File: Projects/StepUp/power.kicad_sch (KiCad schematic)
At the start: 56 parts, among them J10 Conn_02x03_Odd_Even, J11 Conn_01x02, J6 Conn_01x02, J7 Conn_01x02, J8 Conn_01x02, J9 Conn_01x02, Q3 PMF170XP,115, Q4 BSS83P, U6 LDL1117S33R, U7 MCP73832T-2ACI_OT, U8 MIC2253

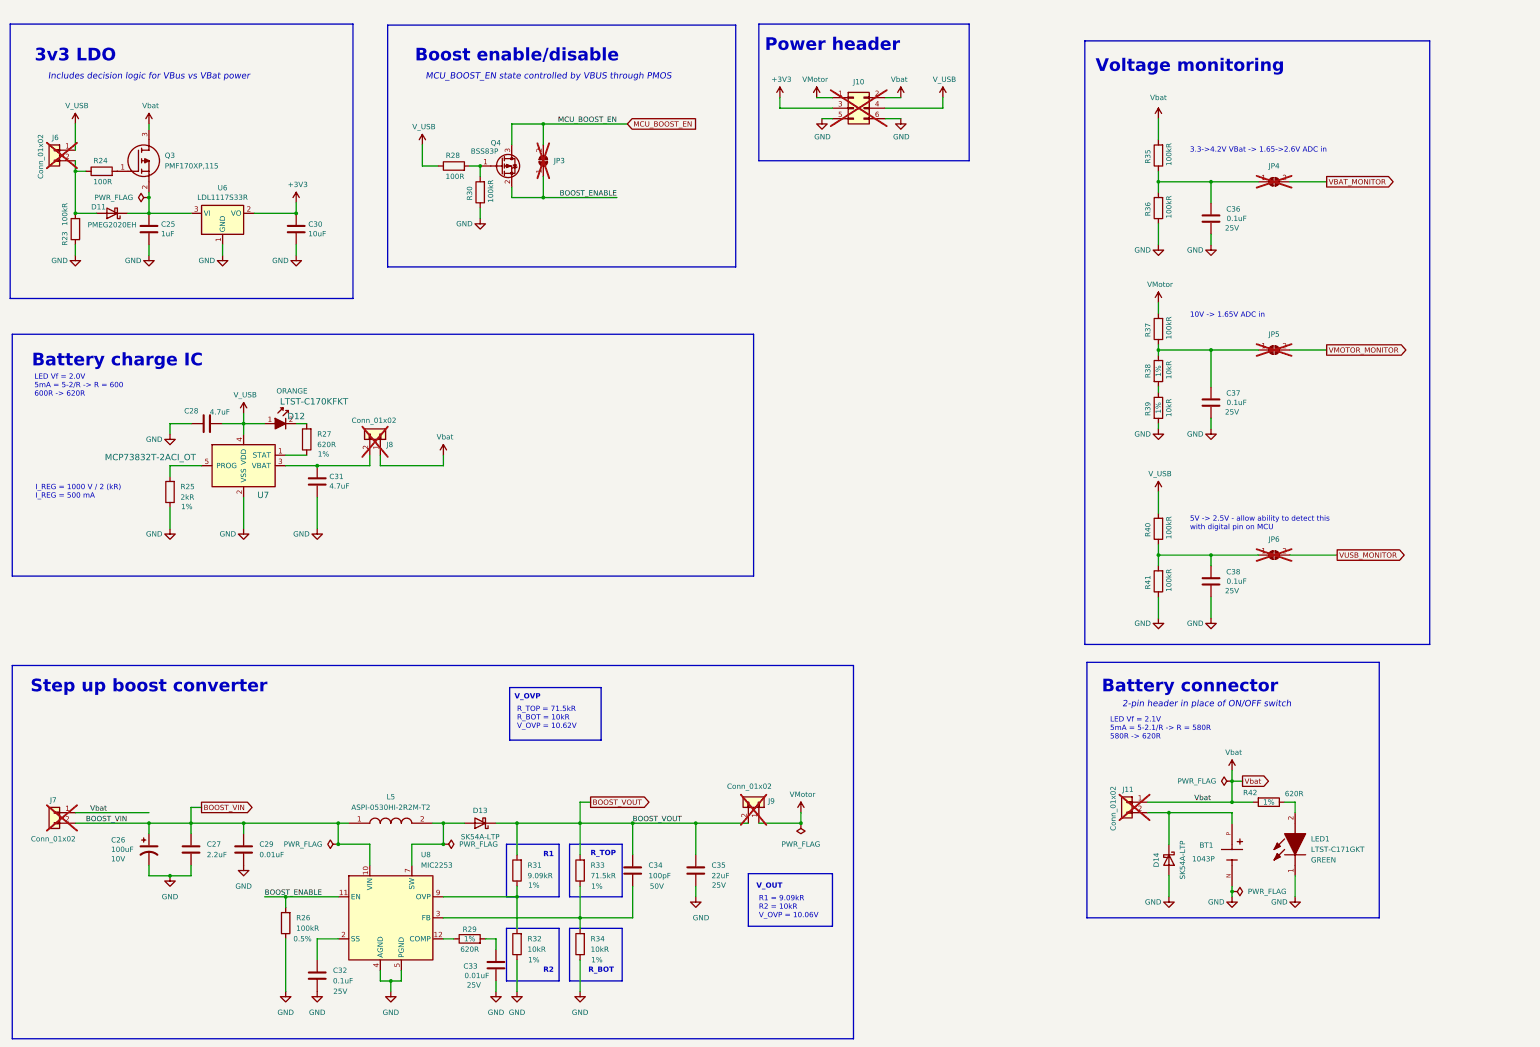
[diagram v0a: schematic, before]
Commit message: feat(v0.2): Schematic updated, PCB layout start
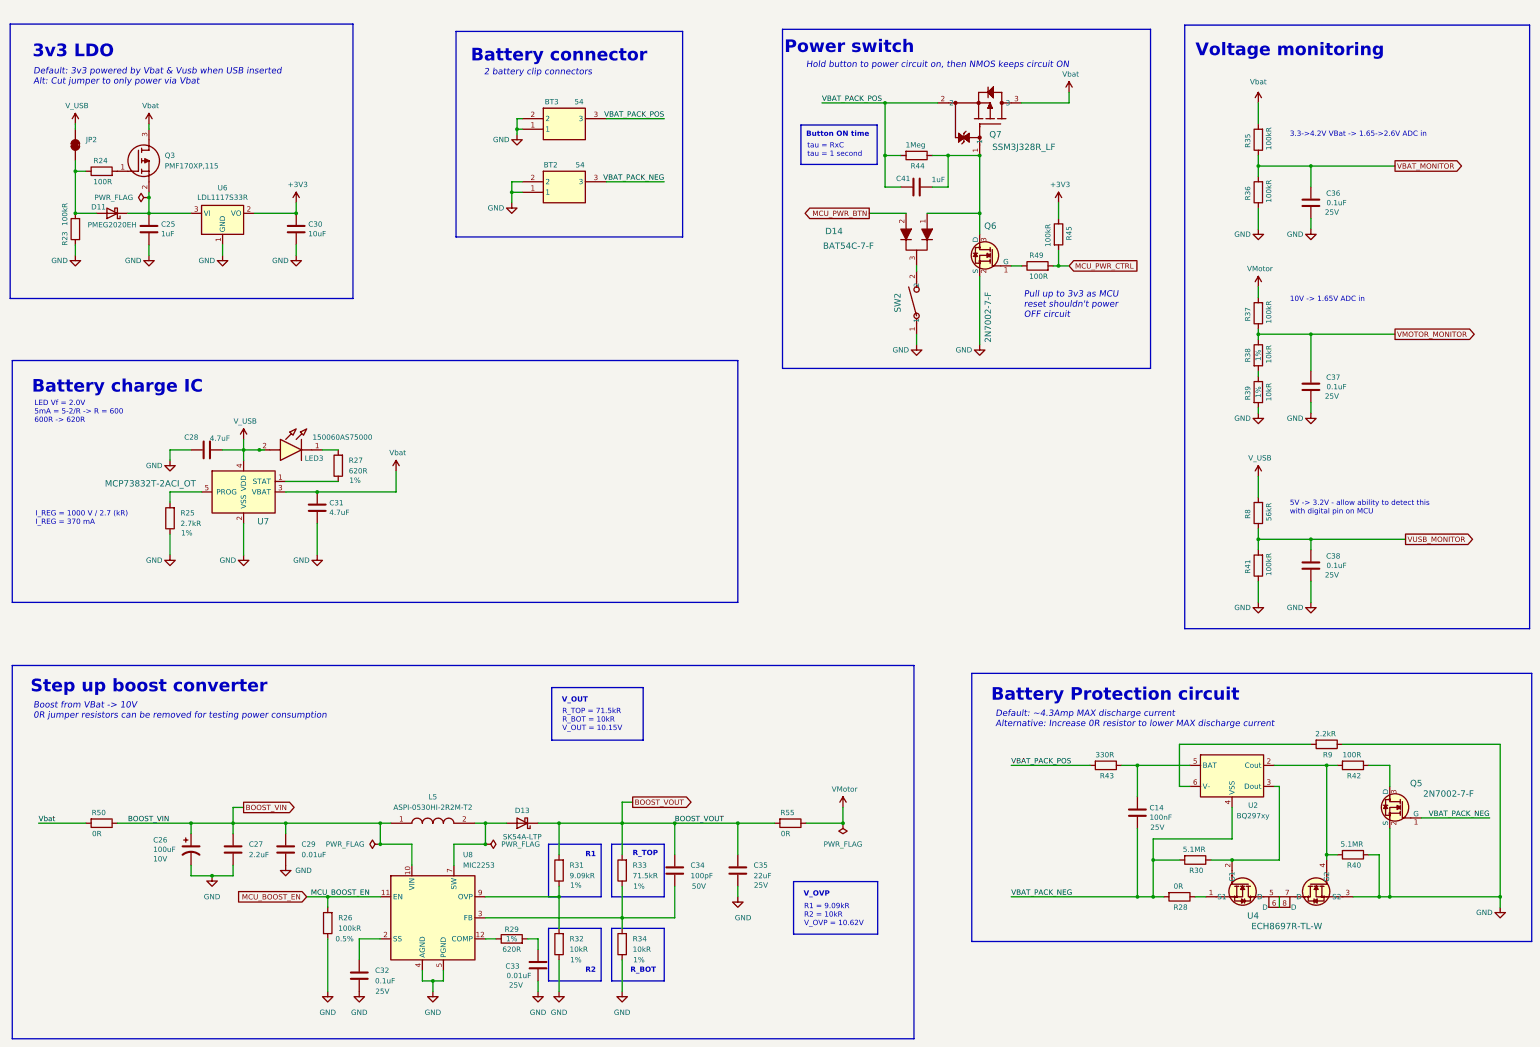
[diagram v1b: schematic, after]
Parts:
- removed BT1: 1043P, Keystone:BAT_1043P, symbol 1043P:1043P
- removed D12: LTST-C170KFKT, digikey-footprints:0805, symbol dk_LED-Indication-Discrete:LTST-C170KFKT
- removed D14: SK54A-LTP, Diode_SMD:D_SMA, symbol Device:D_Schottky
- removed J10: Conn_02x03_Odd_Even, Connector_PinHeader_2.54mm:PinHeader_2x03_P2.54mm_Vertical, symbol Connector_Generic:Conn_02x03_Odd_Even
- removed J11, J6, J7, J8, J9: Conn_01x02, Connector_PinHeader_2.54mm:PinHeader_1x02_P2.54mm_Vertical, symbol Connector_Generic:Conn_01x02
- removed JP3, JP4, JP5, JP6: SolderJumper_2_Open, Jumper:SolderJumper-2_P1.3mm_Open_RoundedPad1.0x1.5mm, symbol Jumper:SolderJumper_2_Open
- removed LED1: LTST-C171GKT, Samacsys:LEDC2012X90N, symbol Samacsys:LTST-C171GKT
- removed Q4: BSS83P, Package_TO_SOT_SMD:SOT-23, symbol Transistor_FET:BSS83P
- added BT2, BT3: 54, Samacsys:54, symbol Samacsys:54
- added C14: 100nF, Capacitor_SMD:C_0402_1005Metric, symbol Device:C
- added C41: 1uF, Capacitor_SMD:C_0603_1608Metric, symbol Device:C
- added D14: BAT54C-7-F, digikey-footprints:SOT-23-3, symbol dk_Diodes-Rectifiers-Arrays:BAT54C-7-F
- added JP2: SolderJumper_2_Bridged, Jumper:SolderJumper-2_P1.3mm_Bridged2Bar_RoundedPad1.0x1.5mm, symbol Jumper:SolderJumper_2_Bridged
- added LED3: 150060AS75000, Samacsys:LEDC1608X80N, symbol Samacsys:150060AS75000
- added Q5, Q6: 2N7002-7-F, digikey-footprints:SOT-23-3, symbol dk_Transistors-FETs-MOSFETs-Single:2N7002-7-F
- added Q7: SSM3J328R_LF, Snapeda:SOT-23F_TOS, symbol Snapeda_kicad:SSM3J328R_LF
- added R43: 330R, Resistor_SMD:R_0603_1608Metric, symbol Device:R
- added R44: 1Meg, Resistor_SMD:R_0603_1608Metric, symbol Device:R
- added R45: 100kR, Resistor_SMD:R_0603_1608Metric, symbol Device:R
- added R49: 100R, Resistor_SMD:R_0603_1608Metric, symbol Device:R
- added R50, R55: 0R, Resistor_SMD:R_0603_1608Metric, symbol Device:R
- added R8: 56kR, Resistor_SMD:R_0603_1608Metric, symbol Device:R
- added R9: 2.2kR, Resistor_SMD:R_0603_1608Metric, symbol Device:R
- added SW2: PTS636SL43SMTRLFS, Snapeda:SW_PTS636S-J_CNK, symbol Snapeda_kicad:PTS636SL43SMTRLFS
- added U2: BQ297xy, Package_SON:WSON-6_1.5x1.5mm_P0.5mm, symbol Battery_Management:BQ297xy
- added U4: ECH8697R-TL-W, Snapeda:SOT-28FL-8_2P9X2P3_ONS, symbol Snapeda_kicad:ECH8697R-TL-W
- R25: value 2kR -> 2.7kR
- R28: value 100R -> 0R; MPN RC0603FR-07100RL -> (none); Manufacturer YAGEO -> (none); Package 0603 -> 0603; Tolerance 1% -> 0.5%
- R30, R40: value 100kR -> 5.1MR; MPN RT0603DRE10100KL -> (none); Manufacturer YAGEO -> (none); Tolerance 0.5% -> (none)
- R42: value 620R -> 100R; MPN RC0603FR-07620RL -> (none); Manufacturer YAGEO -> (none); Tolerance 1% -> (none)
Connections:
- net BOOST_ENABLE is gone; now on net MCU_BOOST_EN: R26.2, U8.11 (EN)
- net +3V3: now also R45.1
- net BOOST_VIN: now also R50.1
- net BOOST_VOUT: now also R55.2
- net GND: now also R40.1, BT2.1, BT2.2, BT3.1, BT3.2, Q5.2 (S), Q6.2 (S), R9.1, SW2.1, U4.3 (S2); no longer R30.1
- net VBAT_MONITOR: now also C36.2, R35.1, R36.2
- net VMOTOR_MONITOR: now also C37.2, R37.1, R38.1
- net VMotor: now also R55.1
- net VUSB_MONITOR: now also C38.2, R41.2, R8.1
- net V_USB: now also JP2.2 (B), LED3.2 (A), R8.2; no longer R28.1, R40.2
- net Vbat: now also C31.1, U7.3 (VBAT), Q7.3, R50.2; no longer R42.2
- net VBAT_PACK_NEG: now reaches R28.2, R30.2
- net VBAT_PACK_NEG: now also BT2.3, C14.2, Q5.1 (G), U2.4 (VSS)
- net at D11.2 (A), R23.2, R24.1: now also JP2.1 (A)
- net at R27.2: now also LED3.1 (K)
- net at R42.1: now also Q5.3 (D)
- new net: Q6.1 (G), R49.1
- new net: C41.2, D14.1, Q6.3 (D), Q7.1, R44.1
- new net: C14.1, R43.1, U2.5 (BAT)
- new net: R9.2, U2.6 (V-)
- new net: D14.3, SW2.2
- new net: R40.2, R42.2, U2.2 (Cout), U4.4 (G2)
- new net: R30.1, U2.3 (Dout), U4.2 (G1)
- new net: R28.1, U4.1 (S1)
- new net: U4.5 (D), U4.6 (D), U4.7 (D), U4.8 (D)
- new net MCU_PWR_BTN: D14.2
- new net MCU_PWR_CTRL: R45.2, R49.2
- new net VBAT_PACK_POS: BT3.3, C41.1, Q7.2, R43.2, R44.2
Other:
- note added: "2 battery clip connectors"
- note added: "5V -> 3.2V - allow ability to detect this with digital pin on MCU"
- note added: "Battery Protection circuit"
- note added: "Boost from VBat -> 10V 0R jumper resistors can be removed for testing power consumption"
- note added: "Button ON time"
- note added: "Default: 3v3 powered by Vbat & Vusb when USB inserted Alt: Cut jumper to only power via Vbat"
- note added: "Default: ~4.3Amp MAX discharge current Alternative: Increase 0R resistor to lower MAX discharge current"
- note added: "Hold button to power circuit on, then NMOS keeps circuit ON"
- note added: "I_REG = 1000 V / 2.7 (kR) I_REG = 370 mA"
- note added: "Power switch"
- note added: "Pull up to 3v3 as MCU reset shouldn't power OFF circuit"
- note added: "R1 = 9.09kR R2 = 10kR V_OVP = 10.62V"
- note added: "R_TOP = 71.5kR R_BOT = 10kR V_OUT = 10.15V"
- note added: "tau = RxC tau = 1 second"
- note removed: "2-pin header in place of ON/OFF switch"
- note removed: "5V -> 2.5V - allow ability to detect this with digital pin on MCU"
- note removed: "Boost enable/disable"
- note removed: "I_REG = 1000 V / 2 (kR) I_REG = 500 mA"
- note removed: "Includes decision logic for VBus vs VBat power"
- note removed: "LED Vf = 2.1V 5mA = 5-2.1/R -> R = 580R 580R -> 620R"
- note removed: "MCU_BOOST_EN state controlled by VBUS through PMOS"
- note removed: "Power header"
- note removed: "R1 = 9.09kR R2 = 10kR V_OVP = 10.06V"
- note removed: "R_TOP = 71.5kR R_BOT = 10kR V_OVP = 10.62V"
- moved on the sheet: C26, C27, C28, C29, C31, C32, C33, C34, C35, C36, C37, C38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

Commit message: feat(v0.2): Rough layout begins
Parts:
- removed LED3: 150060AS75000, Samacsys:LEDC1608X80N, symbol Samacsys:150060AS75000
- removed SW2: PTS636SL43SMTRLFS, Snapeda:SW_PTS636S-J_CNK, symbol Snapeda_kicad:PTS636SL43SMTRLFS
- added LED1: IN-S63AS5A, Samacsys:INS63AS5UW, symbol Samacsys:IN-S63AS5UW
- added SW3: 1825027-8, Samacsys:1825027-8, symbol Samacsys:1825027-8
- U6: renamed from U7; Description_1 (none) -> IC LI-ION/LI-POLY CTRLR SOT23-5; Digi-Key_PN (none) -> MCP73832T-2ACI/OTCT-ND
- renumbered BT3 to BT1, C25 to C24, C26 to C25, C28 to C26, C29 to C28, C30 to C29, C31 to C30, C32 to C31, C33 to C32, C34 to C33, C35 to C34, C41 to C35, C14 to C36, C36 to C37, C37 to C38, C38 to C39, D13 to D12, D14 to D13, JP2 to JP1, Q6 to Q4, Q7 to Q5, Q5 to Q6, R23 to R21, R24 to R22, R50 to R23, R25 to R24, R26 to R25, R27 to R26, R29 to R27, R31 to R28, R32 to R29, R33 to R30, R34 to R31, R55 to R32, R44 to R33, R49 to R34, R45 to R35, R43 to R36, R28 to R37, R30 to R38, R35 to R39, R36 to R40, R37 to R41, R38 to R42, R39 to R43, R8 to R44, R41 to R45, R9 to R46, R42 to R47, R40 to R48, U6 to U5, U8 to U7, U4 to U8, U2 to U9
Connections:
- net GND: now also SW3.1
- net V_USB: now also LED1.2 (A)
- net at R26.2: now also LED1.1 (K)
- net at D13.3: now also SW3.2

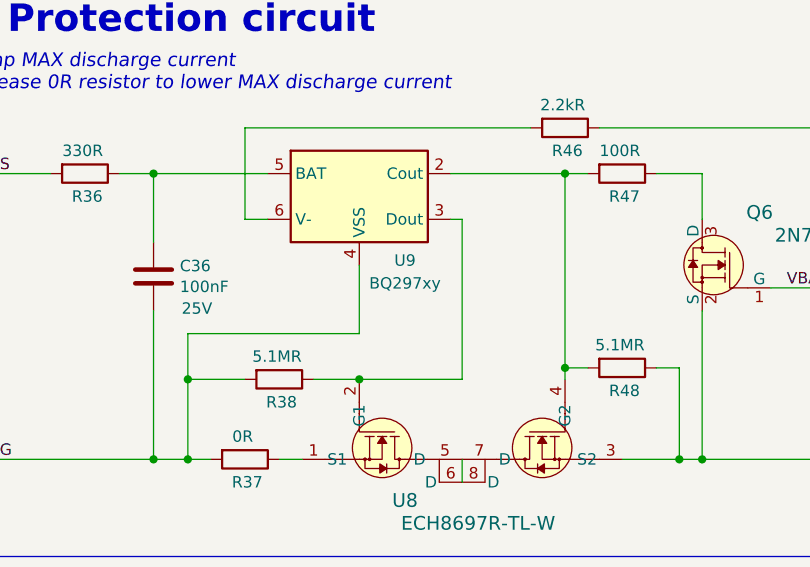
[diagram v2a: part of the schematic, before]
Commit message: feat(v0.2): Component layout from CAD
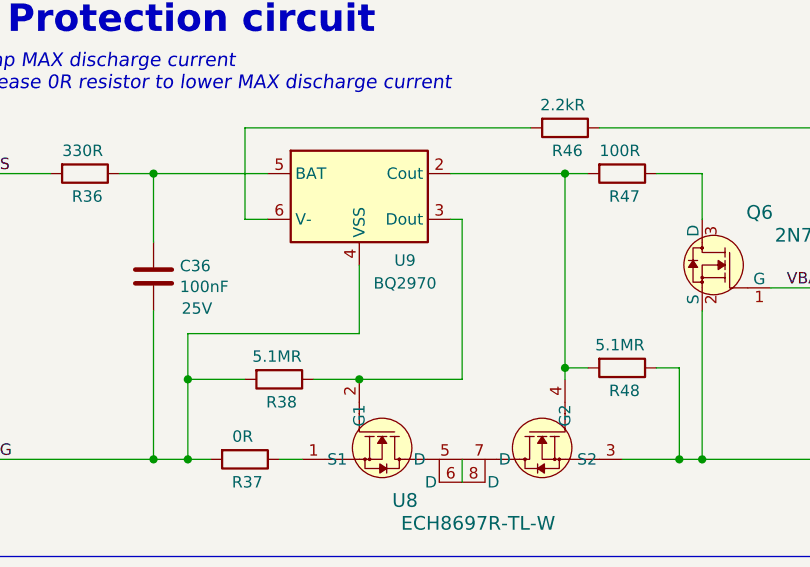
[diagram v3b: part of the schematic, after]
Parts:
- BT1, BT2, SW3: now left out of the parts list
- R23: footprint Resistor_SMD:R_0603_1608Metric -> Resistor_SMD:R_1206_3216Metric
- U9: value BQ297xy -> BQ2970; MPN (none) -> BQ2970; Manufacturer (none) -> Ti
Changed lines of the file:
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@@
 		(unit 1)
 		(exclude_from_sim no)
-		(in_bom yes)
+		(in_bom no)
 		(on_board yes)
 		(dnp no)
@@
 			)
 		)
-		(property "Value" "BQ297xy"
+		(property "Value" "BQ2970"
 			(at 332.74 214.122 0)
 			(effects
@@
 			)
 		)
-		(property "Availability" ""
-			(at 327.66 204.47 0)
-			(effects
-				(font
-					(size 1.27 1.27)
-				)
-				(hide yes)
-			)
-		)
-		(property "Check_prices" ""
-			(at 327.66 204.47 0)
-			(effects
-				(font
-					(size 1.27 1.27)
-				)
-				(hide yes)
-			)
-		)
-		(property "Colour" ""
-			(at 327.66 204.47 0)
-			(effects
-				(font
-					(size 1.27 1.27)
-				)
-				(hide yes)
-			)
-		)
-		(property "MAXIMUM_PACKAGE_HEIGHT" ""
-			(at 327.66 204.47 0)
-			(effects
-				(font
-					(size 1.27 1.27)
-				)
-				(hide yes)
-			)
-		)
-		(property "MP" ""
+		(property "MPN" "BQ2970"
 			(at 327.66 204.47 0)
 			(effects
@@
 			)
 		)
-		(property "PARTREV" ""
-			(at 327.66 204.47 0)
-			(effects
-				(font
-					(size 1.27 1.27)
-				)
-				(hide yes)
-			)
-		)
-		(property "Price" ""
-			(at 327.66 204.47 0)
-			(effects
-				(font
-					(size 1.27 1.27)
-				)
-				(hide yes)
-			)
-		)
-		(property "Purchase-URL" ""
-			(at 327.66 204.47 0)
-			(effects
-				(font
-					(size 1.27 1.27)
-				)
-				(hide yes)
-			)
-		)
-		(property "SNAPEDA_PN" ""
-			(at 327.66 204.47 0)
-			(effects
-				(font
-					(size 1.27 1.27)
-				)
-				(hide yes)
-			)
-		)
-		(property "STANDARD" ""
-			(at 327.66 204.47 0)
-			(effects
-				(font
-					(size 1.27 1.27)
-				)
-				(hide yes)
-			)
-		)
-		(property "SnapEDA_Link" ""
+		(property "Manufacturer" "Ti"
 			(at 327.66 204.47 0)
 			(effects
@@
 		(unit 1)
 		(exclude_from_sim no)
-		(in_bom yes)
+		(in_bom no)
 		(on_board yes)
 		(dnp no)
@@
 			)
 		)
-		(property "Footprint" "Resistor_SMD:R_0603_1608Metric"
+		(property "Footprint" "Resistor_SMD:R_1206_3216Metric"
 			(at 54.61 214.122 90)
 			(effects
@@
 		(unit 1)
 		(exclude_from_sim no)
-		(in_bom yes)
+		(in_bom no)
 		(on_board yes)
 		(dnp no)

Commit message: feat(layout): Layout begins
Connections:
- net GND: no longer BT1.1, BT1.2, BT2.1, BT2.2
- net VBAT_PACK_NEG: now also BT2.1, BT2.2
- net VBAT_PACK_POS: now also BT1.1, BT1.2
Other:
- moved on the sheet: BT1, BT2

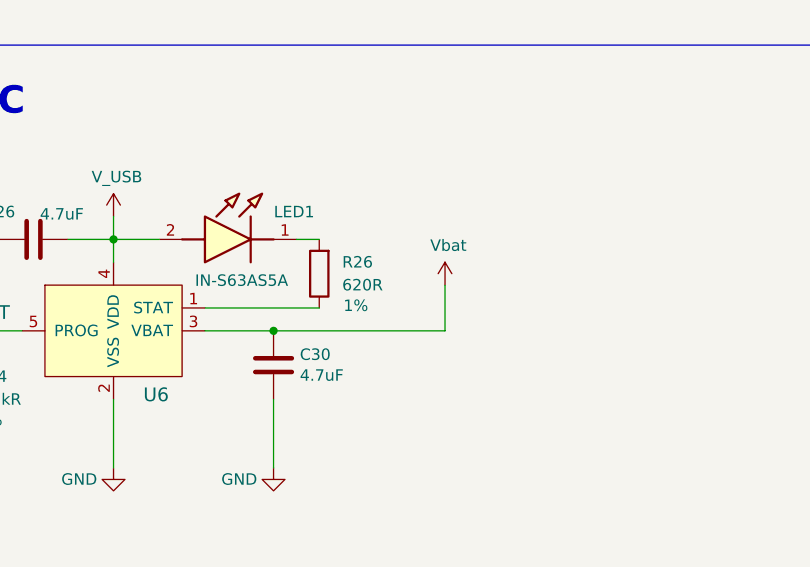
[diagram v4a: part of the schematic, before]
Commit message: feat(layout): Most traces complete
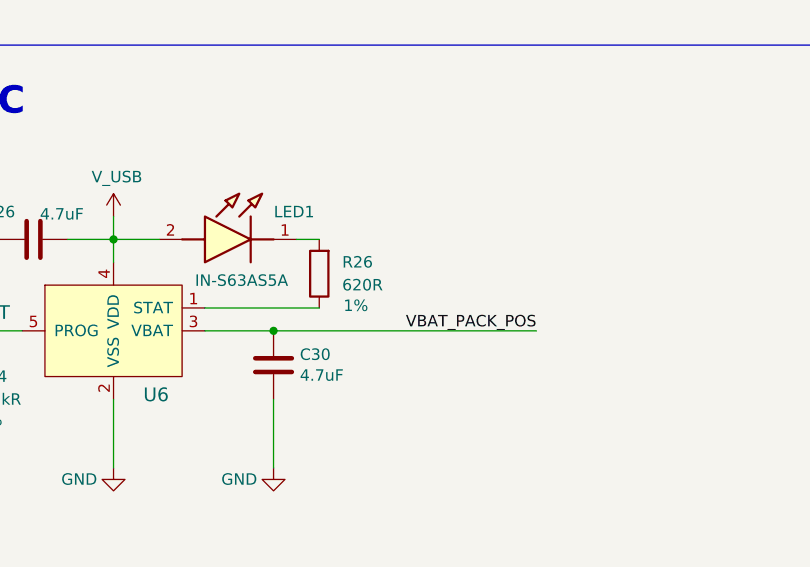
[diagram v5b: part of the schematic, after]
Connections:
- net VBAT_PACK_POS: now also C30.1, U6.3 (VBAT)
- net Vbat: no longer C30.1, U6.3 (VBAT)
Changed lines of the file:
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@@
 	(wire
 		(pts
-			(xy 106.68 135.89) (xy 125.73 135.89)
+			(xy 106.68 135.89) (xy 135.89 135.89)
 		)
 		(stroke
@@
 		(pts
 			(xy 193.04 215.9) (xy 208.28 215.9)
-		)
-		(stroke
-			(width 0)
-			(type default)
-		)
-	)
-	(wire
-		(pts
-			(xy 125.73 130.81) (xy 125.73 135.89)
 		)
 		(stroke
@@
 		)
 	)
+	(label "VBAT_PACK_POS"
+		(at 135.89 135.89 180)
+		(fields_autoplaced yes)
+		(effects
+			(font
+				(size 1.27 1.27)
+			)
+			(justify right bottom)
+		)
+	)
 	(label "VBAT_PACK_NEG"
 		(at 190.5 62.23 180)
@@
 			)
 		)
-	)
-	(symbol
-		(lib_id "power:VBUS")
-		(at 125.73 130.81 0)
-		(unit 1)
-		(exclude_from_sim no)
-		(in_bom yes)
-		(on_board yes)
-		(dnp no)
-		(property "Reference" "#PWR069"
-			(at 125.73 134.62 0)
-			(effects
-				(font
-					(size 1.27 1.27)
-				)
-				(hide yes)
-			)
-		)
-		(property "Value" "Vbat"
-			(at 126.111 126.4158 0)
-			(effects
-				(font
-					(size 1.27 1.27)
-				)
-			)
-		)
-		(property "Footprint" ""
-			(at 125.73 130.81 0)
-			(effects
-				(font
-					(size 1.27 1.27)
-				)
-				(hide yes)
-			)
-		)
-		(property "Datasheet" ""
-			(at 125.73 130.81 0)
-			(effects
-				(font
-					(size 1.27 1.27)
-				)
-				(hide yes)
-			)
-		)
-		(property "Description" "Power symbol creates a global label with name \"VBUS\""
-			(at 125.73 130.81 0)
-			(effects
-				(font
-					(size 1.27 1.27)
-				)
-				(hide yes)
-			)
-		)
-		(pin "1"
-		)
-		(instances
-			(project "StepUp"
-				(path "/e0cca1c7-c263-49eb-8c40-74000ebe5285/e827d0b4-d448-43f9-95b8-3deddd7cd4ee"
-					(reference "#PWR069")
-					(unit 1)
-				)
-			)
-		)
